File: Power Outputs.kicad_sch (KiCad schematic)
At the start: 0 parts

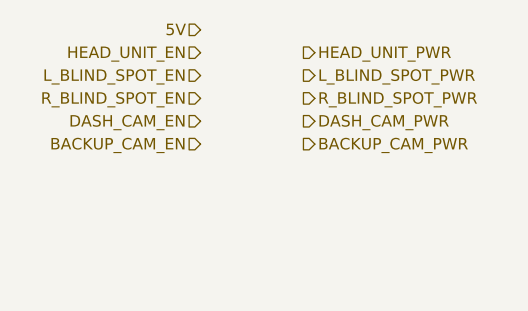
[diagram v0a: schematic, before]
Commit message: power supply circuit schematic done
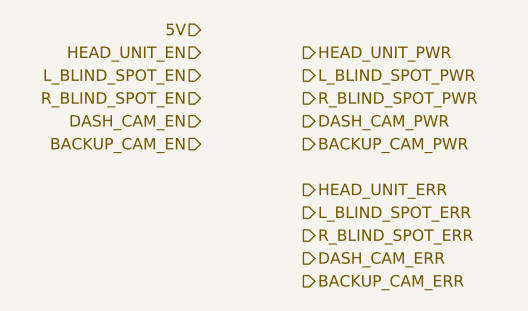
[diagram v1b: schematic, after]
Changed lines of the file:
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@@
     (effects (font (size 1.27 1.27)) (justify right))
+  )
+  (hierarchical_label "DASH_CAM_ERR" (shape output) (at 152.4 99.06 0) (fields_autoplaced)
+    (effects (font (size 1.27 1.27)) (justify left))
   )
   (hierarchical_label "5V" (shape input) (at 140.97 73.66 180) (fields_autoplaced)
@@
   )
   (hierarchical_label "DASH_CAM_PWR" (shape output) (at 152.4 83.82 0) (fields_autoplaced)
+    (effects (font (size 1.27 1.27)) (justify left))
+  )
+  (hierarchical_label "HEAD_UNIT_ERR" (shape output) (at 152.4 91.44 0) (fields_autoplaced)
+    (effects (font (size 1.27 1.27)) (justify left))
+  )
+  (hierarchical_label "BACKUP_CAM_ERR" (shape output) (at 152.4 101.6 0) (fields_autoplaced)
     (effects (font (size 1.27 1.27)) (justify left))
   )
@@
     (effects (font (size 1.27 1.27)) (justify right))
   )
+  (hierarchical_label "L_BLIND_SPOT_ERR" (shape output) (at 152.4 93.98 0) (fields_autoplaced)
+    (effects (font (size 1.27 1.27)) (justify left))
+  )
+  (hierarchical_label "R_BLIND_SPOT_ERR" (shape output) (at 152.4 96.52 0) (fields_autoplaced)
+    (effects (font (size 1.27 1.27)) (justify left))
+  )
   (hierarchical_label "R_BLIND_SPOT_PWR" (shape output) (at 152.4 81.28 0) (fields_autoplaced)

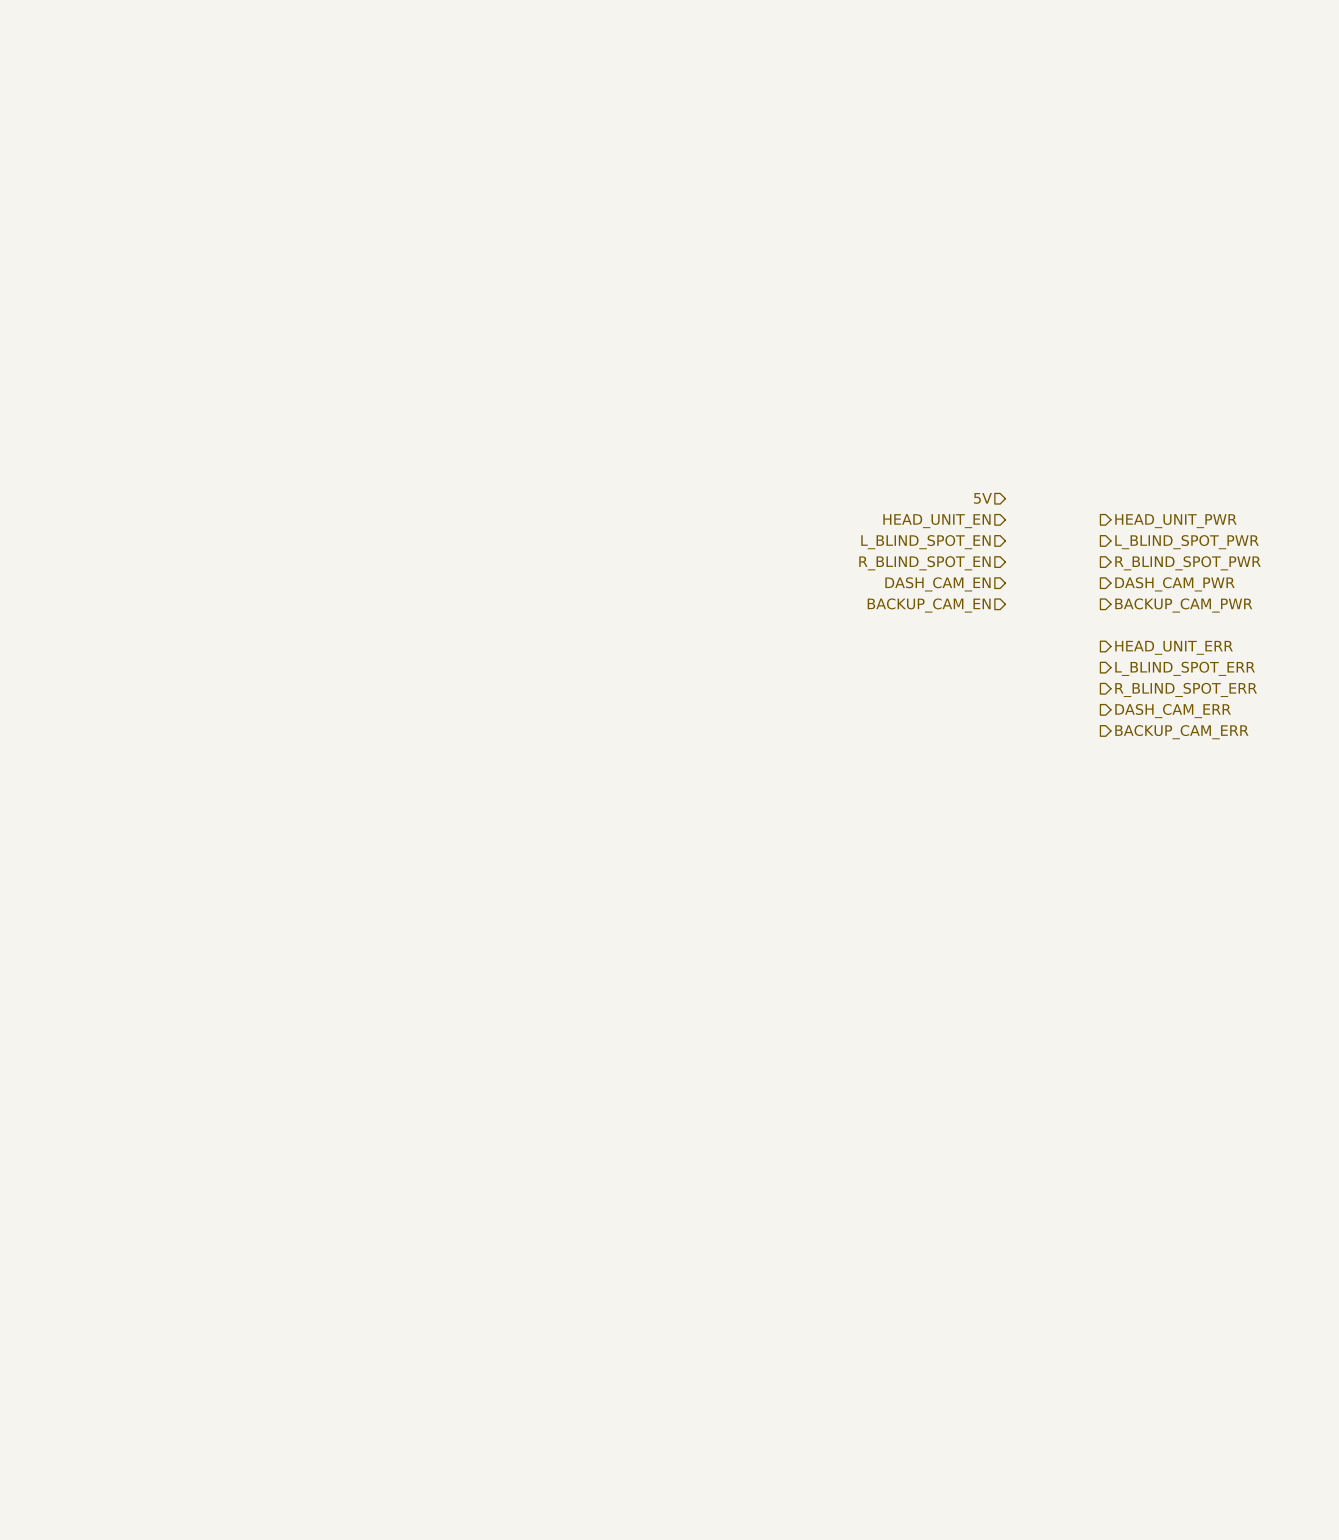
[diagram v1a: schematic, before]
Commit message: working on ignition and power output sheets
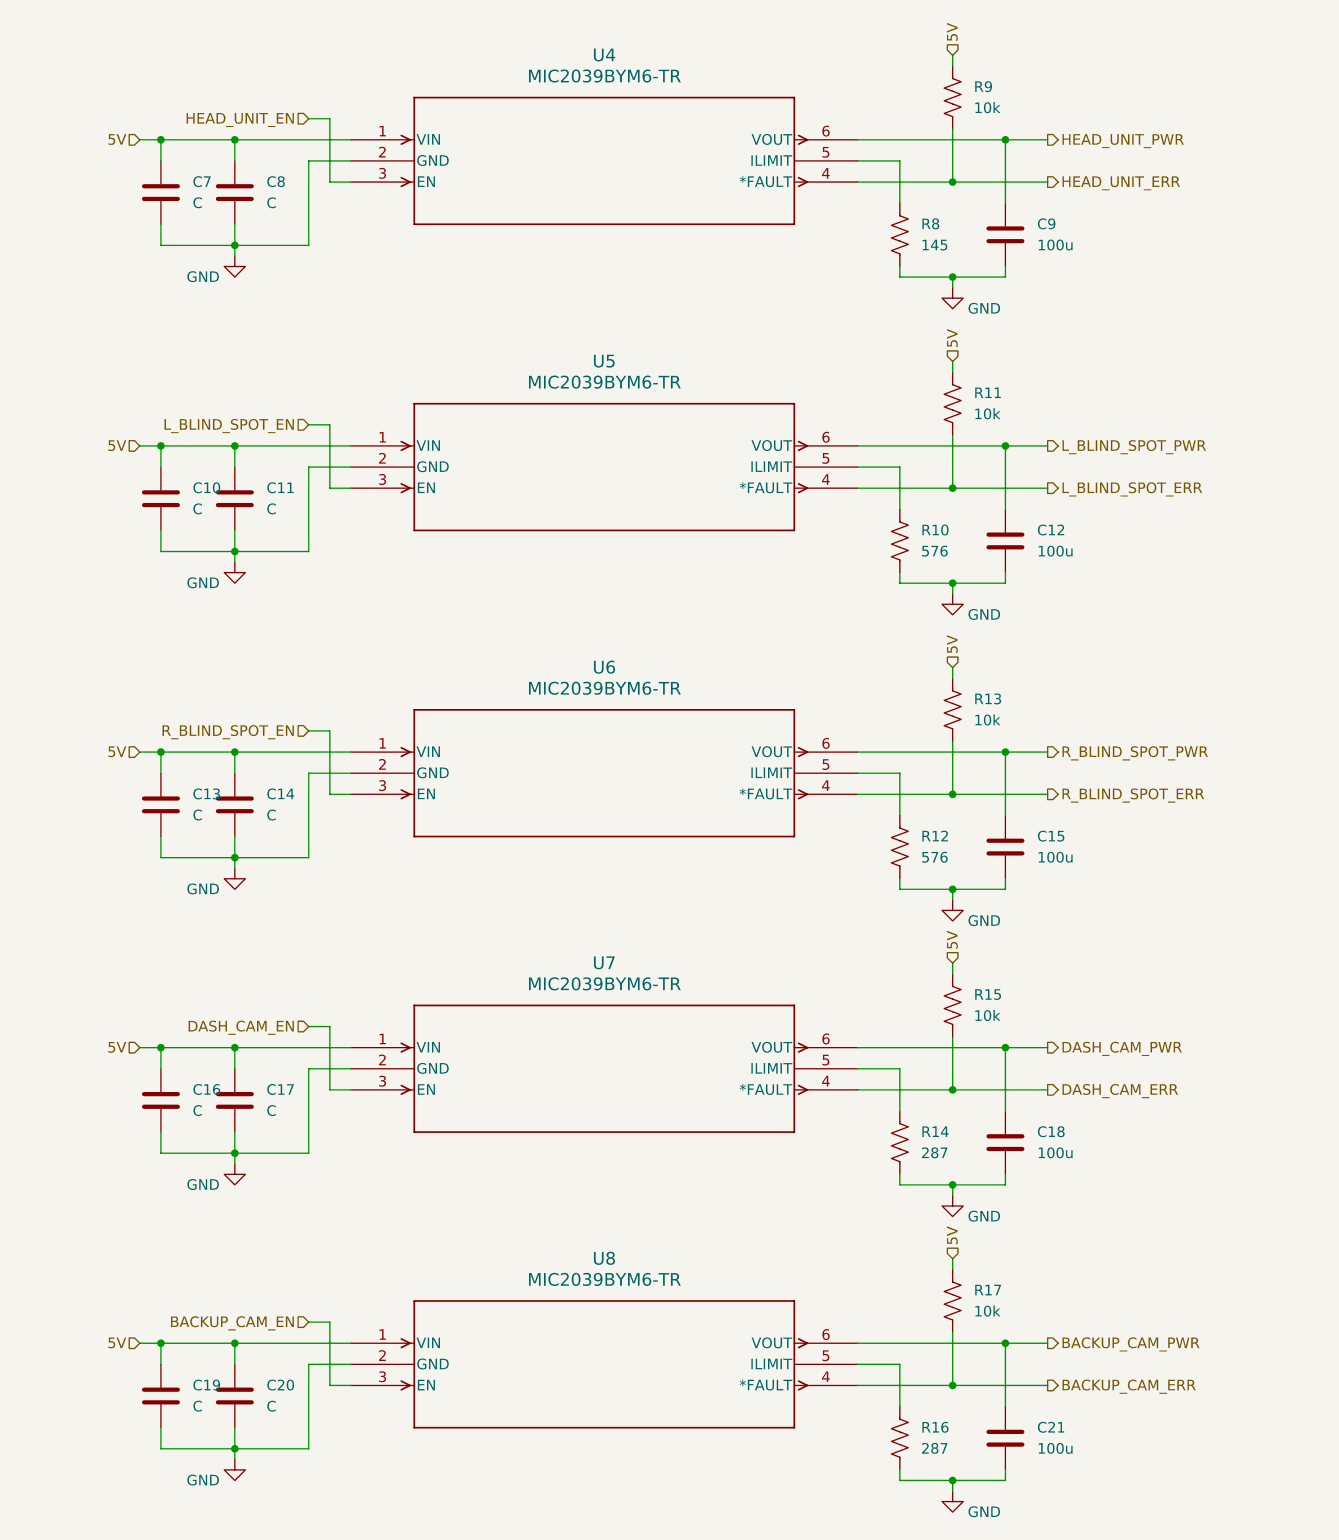
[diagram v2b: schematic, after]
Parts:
- added C10, C11, C13, C14, C16, C17, C19, C20, C7, C8: C, symbol Device:C
- added C12, C15, C18, C21, C9: 100u, symbol Device:C
- added R10, R12: 576, symbol Device:R_US
- added R11, R13, R15, R17, R9: 10k, symbol Device:R_US
- added R14, R16: 287, symbol Device:R_US
- added R8: 145, symbol Device:R_US
- added U4, U5, U6, U7, U8: MIC2039BYM6-TR, SOT-23-6_M6_MCH, symbol MIC2039BYM6_TR:MIC2039BYM6-TR
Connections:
- net 5V: now also C10.1, C11.1, C13.1, C14.1, C16.1, C17.1, C19.1, C20.1, C7.1, C8.1, R11.1, R13.1, R15.1, R17.1, R9.1, U4.1 (VIN), U5.1 (VIN), U6.1 (VIN), U7.1 (VIN), U8.1 (VIN)
- net BACKUP_CAM_EN: now also U8.3 (EN)
- net BACKUP_CAM_ERR: now also R17.2, U8.4 (*FAULT)
- net BACKUP_CAM_PWR: now also C21.1, U8.6 (VOUT)
- net DASH_CAM_EN: now also U7.3 (EN)
- net DASH_CAM_ERR: now also R15.2, U7.4 (*FAULT)
- net DASH_CAM_PWR: now also C18.1, U7.6 (VOUT)
- net HEAD_UNIT_EN: now also U4.3 (EN)
- net HEAD_UNIT_ERR: now also R9.2, U4.4 (*FAULT)
- net HEAD_UNIT_PWR: now also C9.1, U4.6 (VOUT)
- net L_BLIND_SPOT_EN: now also U5.3 (EN)
- net L_BLIND_SPOT_ERR: now also R11.2, U5.4 (*FAULT)
- net L_BLIND_SPOT_PWR: now also C12.1, U5.6 (VOUT)
- net R_BLIND_SPOT_EN: now also U6.3 (EN)
- net R_BLIND_SPOT_ERR: now also R13.2, U6.4 (*FAULT)
- net R_BLIND_SPOT_PWR: now also C15.1, U6.6 (VOUT)
- new net: R10.1, U5.5 (ILIMIT)
- new net: R12.1, U6.5 (ILIMIT)
- new net: R8.1, U4.5 (ILIMIT)
- new net: R16.1, U8.5 (ILIMIT)
- new net: R14.1, U7.5 (ILIMIT)
- new net GND: C10.2, C11.2, C12.2, C13.2, C14.2, C15.2, C16.2, C17.2, C18.2, C19.2, C20.2, C21.2, C7.2, C8.2, C9.2, R10.2, R12.2, R14.2, R16.2, R8.2, U4.2 (GND), U5.2 (GND), U6.2 (GND), U7.2 (GND), U8.2 (GND)

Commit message: switch Ignition page to use load drivers rather than discrete FETs
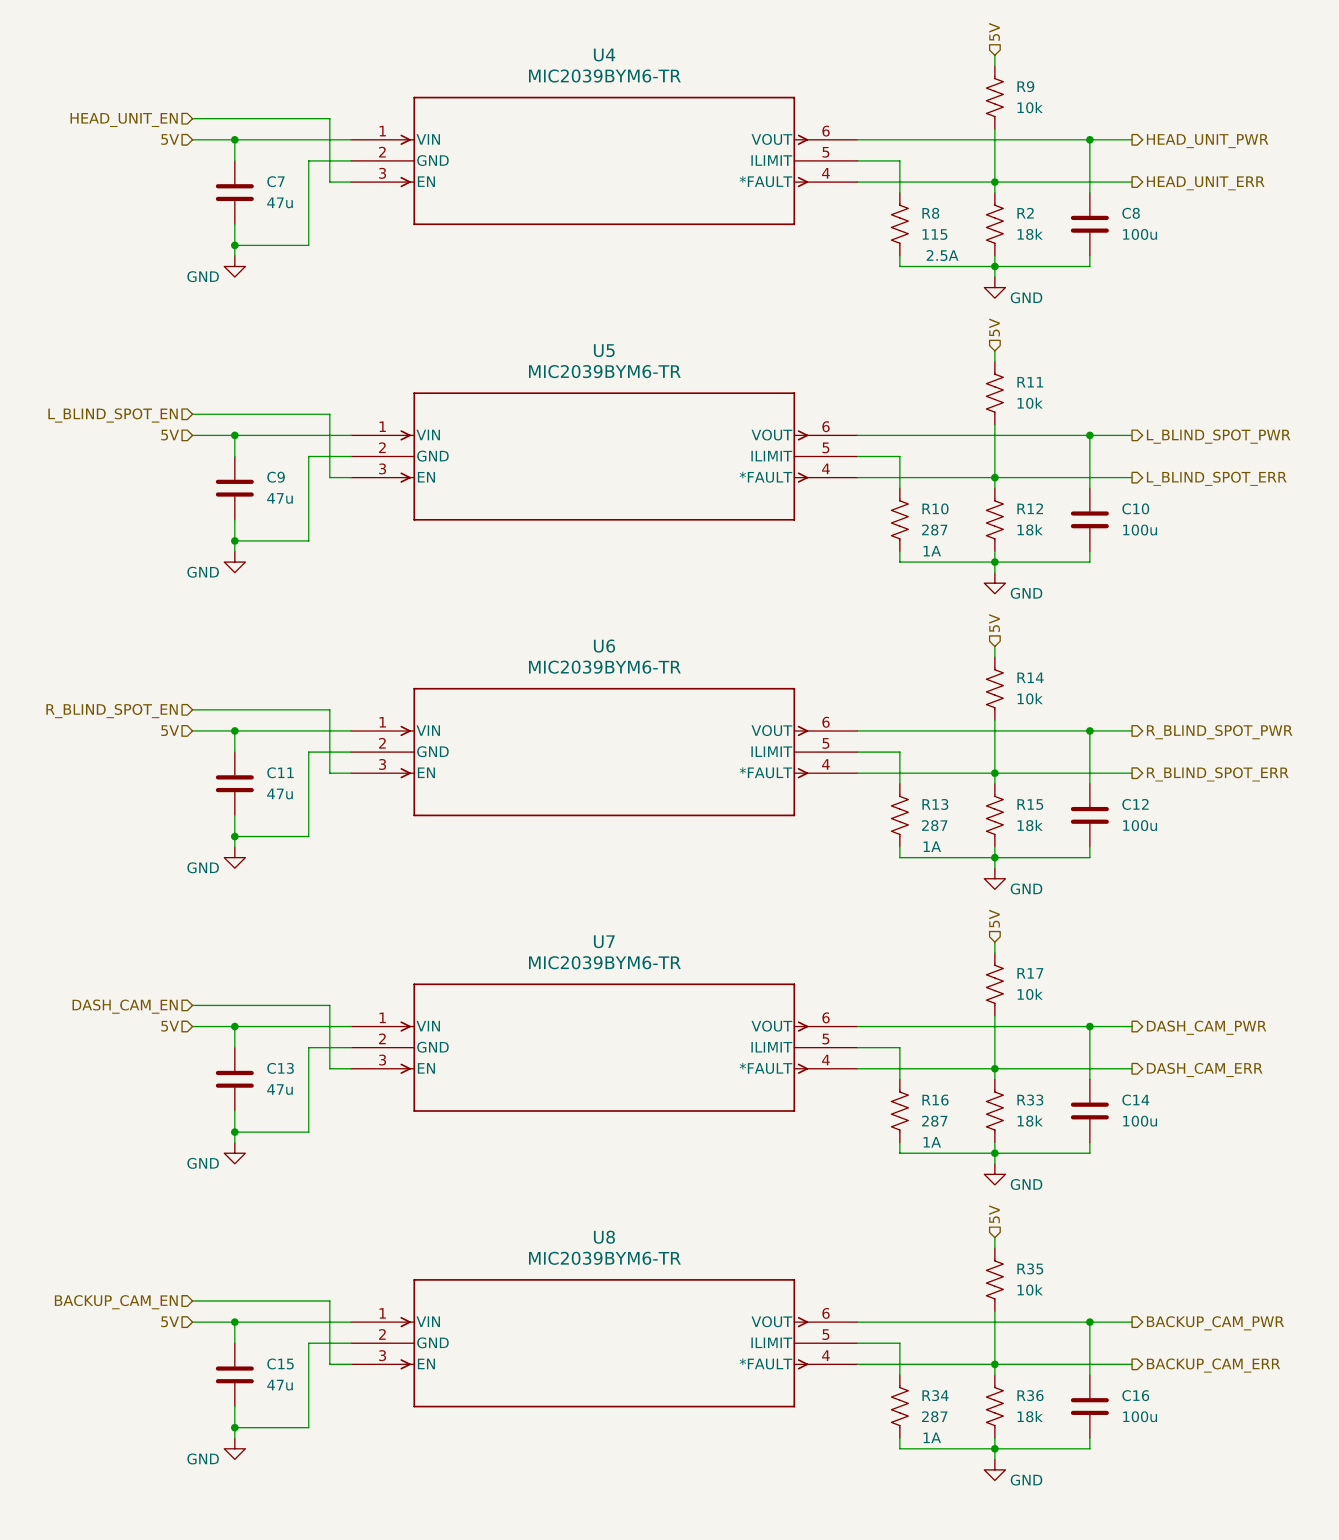
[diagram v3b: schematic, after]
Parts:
- removed C17, C19, C20, C8: C, symbol Device:C
- removed C18, C21: 100u, symbol Device:C
- added C9: 47u, symbol Device:C
- added R2, R33, R36: 18k, symbol Device:R_US
- added R34: 287, symbol Device:R_US
- added R35: 10k, symbol Device:R_US
- C10, C14, C16: value C -> 100u
- C11, C13, C7: value C -> 47u
- C15: value 100u -> 47u
- R10: value 576 -> 287; Current Limit (none) -> 1A
- R12: value 576 -> 18k
- R13: value 10k -> 287; Current Limit (none) -> 1A
- R14: value 287 -> 10k
- R15: value 10k -> 18k
- R16: Current Limit (none) -> 1A
- R8: value 145 -> 115; Current Limit (none) -> 2.5A
- renumbered C9 to C8
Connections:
- net 5V: now also C15.1, R14.1, C9.1, R35.1; no longer C10.1, C14.1, C16.1, R13.1, R15.1
- net BACKUP_CAM_ERR: now also R35.2, R36.1; no longer R17.2
- net BACKUP_CAM_PWR: now also C16.1
- net DASH_CAM_ERR: now also R17.2, R33.1; no longer R15.2
- net DASH_CAM_PWR: now also C14.1
- net GND: now also R13.2, R15.2, C9.2, R2.2, R33.2, R34.2, R36.2; no longer R14.2
- net HEAD_UNIT_ERR: now also R2.1
- net L_BLIND_SPOT_ERR: now also R12.1
- net L_BLIND_SPOT_PWR: now also C10.1; no longer C12.1
- net R_BLIND_SPOT_ERR: now also R14.2, R15.1; no longer R13.2
- net R_BLIND_SPOT_PWR: now also C12.1; no longer C15.1
- net at U6.5 (ILIMIT): now also R13.1; no longer R12.1
- net at U8.5 (ILIMIT): now also R34.1; no longer R16.1
- net at U7.5 (ILIMIT): now also R16.1; no longer R14.1
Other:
- company: (none) -> J2B
- moved on the sheet: C7, C8, R8, R9
